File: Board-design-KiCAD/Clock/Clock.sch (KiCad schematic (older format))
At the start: 32 parts, among them M1 SevSeg4Inch, M2 SevSeg4Inch, U1 ULN2003A, U2 ULN2003A, U3 74HC595, U4 74HC595, U6 74HC595, Y1 SevSeg1.8Inch, Y2 SevSeg1.8Inch, Y3 SevSeg1.8Inch, Y4 SevSeg1.8Inch

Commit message: Add new tracks
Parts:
- added 5V-Cin1: 0.22uF - 50V, Capacitor_THT:CP_Radial_D4.0mm_P2.00mm, symbol Device:CP1
- added 5V-Cout1, 6V-Cout1: 0.1uF - 50V, Capacitor_THT:CP_Radial_D5.0mm_P2.00mm, symbol Device:CP1
- added 6V-Cin1: 0.33uF - 50V, Capacitor_THT:CP_Radial_D4.0mm_P2.00mm, symbol Device:CP1
- added CommonPinControl_YEAR1: ULN2003A, Package_DIP:DIP-16_W7.62mm_Socket_LongPads, symbol Transistor_Array:ULN2003A
- added RDP1, RDP2: 680, Resistor_THT:R_Axial_DIN0207_L6.3mm_D2.5mm_P10.16mm_Horizontal, symbol Device:R_US
- added Regulator-5V1: LM7805_TO220, Package_TO_SOT_THT:TO-220-3_Horizontal_TabDown, symbol Regulator_Linear:LM7805_TO220
- added Regulator-6V1: L7806, Package_TO_SOT_THT:TO-220-3_Horizontal_TabDown, symbol Regulator_Linear:L7806
- BCD-TIME1: renamed from BCD-YEAR1; footprint Package_DIP:DIP-18_W7.62mm_LongPads -> Package_DIP:DIP-16_W7.62mm_Socket_LongPads
- CommonPinControl_TIME1: renamed from CommonPinControl1; footprint Package_DIP:DIP-18_W7.62mm_LongPads -> Package_DIP:DIP-16_W7.62mm_Socket_LongPads
- DATE_INPUT_CONTROL1: renamed from U6; footprint (none) -> Package_DIP:DIP-16_W7.62mm_Socket_LongPads
- InputPowerConverter1: footprint Package_DIP:DIP-18_W7.62mm_LongPads -> Package_DIP:DIP-16_W7.62mm_Socket_LongPads
- TIME_INPUT_CONTROL1: renamed from U3; footprint (none) -> Package_DIP:DIP-16_W7.62mm_Socket_LongPads
- YEAR_INPUT_CONTROL1: renamed from U4; footprint (none) -> Package_DIP:DIP-16_W7.62mm_Socket_LongPads
- renumbered BCD-TIME1 to BCD-YEAR1
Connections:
- net +11V: now also 5V-Cin1.1, 6V-Cin1.1, Regulator-5V1.1 (VI), Regulator-6V1.1 (IN)
- net GND: now also BCD-YEAR1.8 (GND), TIME_INPUT_CONTROL1.8 (GND), YEAR_INPUT_CONTROL1.8 (GND), 5V-Cin1.2, 5V-Cout1.2, 6V-Cin1.2, 6V-Cout1.2, CommonPinControl_YEAR1.8 (GND), Regulator-5V1.2 (GND), Regulator-6V1.2 (GND)
- net H1_EN: now reaches H1.1 (GND), H1.8 (GND)
- net H1_EN: now also CommonPinControl_TIME1.16 (O1)
- net H2_EN: now reaches H2.1 (GND), H2.8 (GND)
- net H2_EN: now also CommonPinControl_TIME1.15 (O2)
- net at H2.5 (DP): now also RDP1.1
- net H3_EN: now reaches M1.1 (GND), M1.8 (GND)
- net H3_EN: now also CommonPinControl_TIME1.14 (O3)
- net at M1.5 (DP): now also RDP2.1
- net H4_EN: now reaches M2.1 (GND), M2.8 (GND)
- net H4_EN: now also CommonPinControl_TIME1.13 (O4)
- net Y1_EN: now reaches Y1.1 (Vdd), Y1.5 (Vdd)
- net Y1_EN: now also CommonPinControl_YEAR1.16 (O1)
- net YEAR_G: now reaches Y1.10 (G)
- net YEAR_G: now also BCD-YEAR1.14 (g), Y2.10 (G), Y3.10 (G), Y4.10 (G)
- net YEAR_E: now reaches Y1.2 (E)
- net YEAR_E: now also BCD-YEAR1.9 (e), Y2.2 (E), Y3.2 (E), Y4.2 (E)
- net YEAR_D: now reaches Y1.3 (D)
- net YEAR_D: now also BCD-YEAR1.10 (d), Y2.3 (D), Y3.3 (D), Y4.3 (D)
- net YEAR_C: now reaches Y1.4 (C)
- net YEAR_C: now also BCD-YEAR1.11 (c), Y2.4 (C), Y3.4 (C), Y4.4 (C)
- net YEAR_B: now reaches Y1.6 (B)
- net YEAR_B: now also BCD-YEAR1.12 (b), Y2.6 (B), Y3.6 (B), Y4.6 (B)
- net YEAR_A: now reaches Y1.7 (A)
- net YEAR_A: now also BCD-YEAR1.13 (a), Y2.7 (A), Y3.7 (A), Y4.7 (A)
- net YEAR_F: now reaches Y1.9 (F)
- net YEAR_F: now also BCD-YEAR1.15 (f), Y2.9 (F), Y3.9 (F), Y4.9 (F)
- net Y2_EN: now reaches Y2.1 (Vdd), Y2.5 (Vdd)
- net Y2_EN: now also CommonPinControl_YEAR1.15 (O2)
- net Y3_EN: now reaches Y3.1 (Vdd), Y3.5 (Vdd)
- net Y3_EN: now also CommonPinControl_YEAR1.14 (O3)
- net Y4_EN: now reaches Y4.1 (Vdd), Y4.5 (Vdd)
- net Y4_EN: now also CommonPinControl_YEAR1.13 (O4)
- net at BCD-TIME1.1 (B): now also TIME_INPUT_CONTROL1.1 (QB)
- net +6V: now reaches BCD-TIME1.16 (VCC)
- net +6V: now also BCD-YEAR1.16 (VCC), 6V-Cout1.1, CommonPinControl_YEAR1.9 (COM), Regulator-6V1.3 (OUT)
- net at BCD-TIME1.2 (C): now also TIME_INPUT_CONTROL1.2 (QC)
- net +5V: now reaches BCD-TIME1.3 (LT)
- net +5V: now also BCD-TIME1.4 (BI), BCD-TIME1.5 (RBI), BCD-YEAR1.3 (LT), BCD-YEAR1.4 (BI), BCD-YEAR1.5 (RBI), TIME_INPUT_CONTROL1.16 (VCC), YEAR_INPUT_CONTROL1.16 (VCC), 5V-Cout1.1, Regulator-5V1.3 (VO)
- net at BCD-TIME1.6 (D): now also TIME_INPUT_CONTROL1.3 (QD)
- net at BCD-TIME1.7 (A): now also TIME_INPUT_CONTROL1.15 (QA)
- net at YEAR_INPUT_CONTROL1.1 (QB): now also BCD-YEAR1.1 (B)
- net at YEAR_INPUT_CONTROL1.15 (QA): now also BCD-YEAR1.7 (A)
- net at YEAR_INPUT_CONTROL1.2 (QC): now also BCD-YEAR1.2 (C)
- net at YEAR_INPUT_CONTROL1.3 (QD): now also BCD-YEAR1.6 (D)
- net EN_DIGIT_1: now reaches CommonPinControl_TIME1.1 (I1)
- net DP_EN: now reaches CommonPinControl_TIME1.12 (O5)
- net DP_EN: now also RDP1.2, RDP2.2
- net EN_DIGIT_2: now reaches CommonPinControl_TIME1.2 (I2)
- net EN_DIGIT_3: now reaches CommonPinControl_TIME1.3 (I3)
- net EN_DIGIT_4: now reaches CommonPinControl_TIME1.4 (I4)
- new net INVERTED_EN_DIGIT_1: CommonPinControl_YEAR1.1 (I1)
- new net INVERTED_EN_DIGIT_2: CommonPinControl_YEAR1.2 (I2)
- new net INVERTED_EN_DIGIT_3: CommonPinControl_YEAR1.3 (I3)
- new net INVERTED_EN_DIGIT_4: CommonPinControl_YEAR1.4 (I4)
- no-connect marks 11 -> 21
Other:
- moved on the sheet: BCD-TIME1, BCD-YEAR1, Cff1, Cin1, CommonPinControl_TIME1, Cout1, DATE_INPUT_CONTROL1, Diode1, H1, H2, InputPowerConverter1, L1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

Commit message: Add some display wirings
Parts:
- removed D1, D2, Mo1, Mo2: SevSeg1.8Inch, Custom:SevSeg1.8Inch, symbol Custom:SevSeg1.8Inch
- removed U1, U2: ULN2003A, symbol Transistor_Array:ULN2003A
- added CommonPinControl_DATE1: ULN2003A, Package_DIP:DIP-16_W7.62mm_Socket_LongPads, symbol Transistor_Array:ULN2003A
- added Da_1, Da_2, Mo_1, Mo_2: SevSeg1.8Inch, Custom:SevSeg1.8Inch, symbol Custom:SevSeg1.8Inch
- added INVERTER_1, INVERTER_2: 74HC14, Package_DIP:DIP-14_W7.62mm_Socket_LongPads, symbol 74xx:74HC14
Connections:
- net INVERTED_EN_DIGIT_1 is gone; now on net EN_DIGIT_1: CommonPinControl_YEAR1.1 (I1)
- net INVERTED_EN_DIGIT_2 is gone; now on net EN_DIGIT_2: CommonPinControl_YEAR1.2 (I2)
- net INVERTED_EN_DIGIT_3 is gone; now on net EN_DIGIT_3: CommonPinControl_YEAR1.3 (I3)
- net INVERTED_EN_DIGIT_4 is gone; now on net EN_DIGIT_4: CommonPinControl_YEAR1.4 (I4)
- net +5V: now also BCD-TIME1.16 (VCC), DATE_INPUT_CONTROL1.10 (~SRCLR), DATE_INPUT_CONTROL1.16 (VCC), TIME_INPUT_CONTROL1.10 (~SRCLR), YEAR_INPUT_CONTROL1.10 (~SRCLR), INVERTER_1.14 (VCC), INVERTER_2.14 (VCC); no longer BCD-YEAR1.3 (LT), BCD-YEAR1.4 (BI), BCD-YEAR1.5 (RBI)
- net +6V: now also BCD-DATE1.16 (VCC), BCD-DATE1.3 (LT), BCD-DATE1.4 (BI), BCD-DATE1.5 (RBI), BCD-YEAR1.3 (LT), BCD-YEAR1.4 (BI), BCD-YEAR1.5 (RBI), CommonPinControl_DATE1.9 (COM); no longer BCD-TIME1.16 (VCC)
- net EN_DIGIT_1: now also CommonPinControl_DATE1.1 (I1), INVERTER_2.3; no longer CommonPinControl_TIME1.1 (I1)
- net EN_DIGIT_2: now also CommonPinControl_DATE1.2 (I2), INVERTER_2.5; no longer CommonPinControl_TIME1.2 (I2)
- net EN_DIGIT_3: now also CommonPinControl_DATE1.3 (I3), INVERTER_2.9; no longer CommonPinControl_TIME1.3 (I3)
- net EN_DIGIT_4: now also CommonPinControl_DATE1.4 (I4), INVERTER_2.11; no longer CommonPinControl_TIME1.4 (I4)
- net GND: now also BCD-DATE1.8 (GND), DATE_INPUT_CONTROL1.13 (~OE), DATE_INPUT_CONTROL1.8 (GND), TIME_INPUT_CONTROL1.13 (~OE), YEAR_INPUT_CONTROL1.13 (~OE), CommonPinControl_DATE1.8 (GND), INVERTER_1.7 (GND), INVERTER_2.7 (GND)
- net PWR_TIME_D: now reaches InputPowerConverter1.4 (I4)
- net PWR_TIME_D: now also INVERTER_1.8; no longer BCD-TIME1.10 (d)
- net PWR_TIME_C: now reaches InputPowerConverter1.3 (I3)
- net PWR_TIME_C: now also INVERTER_1.6; no longer BCD-TIME1.11 (c)
- net PWR_TIME_B: now reaches InputPowerConverter1.2 (I2)
- net PWR_TIME_B: now also INVERTER_1.4; no longer BCD-TIME1.12 (b)
- net PWR_TIME_A: now reaches InputPowerConverter1.1 (I1)
- net PWR_TIME_A: now also INVERTER_1.2; no longer BCD-TIME1.13 (a)
- net PWR_TIME_G: now reaches InputPowerConverter1.7 (I7)
- net PWR_TIME_G: now also INVERTER_2.2; no longer BCD-TIME1.14 (g)
- net PWR_TIME_F: now reaches InputPowerConverter1.6 (I6)
- net PWR_TIME_F: now also INVERTER_1.12; no longer BCD-TIME1.15 (f)
- net PWR_TIME_E: now reaches InputPowerConverter1.5 (I5)
- net PWR_TIME_E: now also INVERTER_1.10; no longer BCD-TIME1.9 (e)
- net CLOCK: now reaches TIME_INPUT_CONTROL1.11 (SRCLK)
- net CLOCK: now also DATE_INPUT_CONTROL1.11 (SRCLK), YEAR_INPUT_CONTROL1.11 (SRCLK)
- net LATCH: now reaches TIME_INPUT_CONTROL1.12 (RCLK)
- net LATCH: now also DATE_INPUT_CONTROL1.12 (RCLK), YEAR_INPUT_CONTROL1.12 (RCLK)
- net TIME_DATA_INPUT: now reaches TIME_INPUT_CONTROL1.14 (SER)
- net YEAR_DATA_INPUT: now reaches YEAR_INPUT_CONTROL1.14 (SER)
- net at DATE_INPUT_CONTROL1.1 (QB): now also BCD-DATE1.1 (B)
- net DATE_DATA_INPUT: now reaches DATE_INPUT_CONTROL1.14 (SER)
- net at DATE_INPUT_CONTROL1.15 (QA): now also BCD-DATE1.7 (A)
- net at DATE_INPUT_CONTROL1.2 (QC): now also BCD-DATE1.2 (C)
- net at DATE_INPUT_CONTROL1.3 (QD): now also BCD-DATE1.6 (D)
- net DP_PWM: now reaches CommonPinControl_TIME1.5 (I5)
- net DATE_D: now reaches BCD-DATE1.10 (d)
- net DATE_D: now also Da_1.3 (D), Da_2.3 (D), Mo_1.3 (D), Mo_2.3 (D)
- net DATE_C: now reaches BCD-DATE1.11 (c)
- net DATE_C: now also Da_1.4 (C), Da_2.4 (C), Mo_1.4 (C), Mo_2.4 (C)
- net DATE_B: now reaches BCD-DATE1.12 (b)
- net DATE_B: now also Da_1.6 (B), Da_2.6 (B), Mo_1.6 (B), Mo_2.6 (B)
- net DATE_A: now reaches BCD-DATE1.13 (a)
- net DATE_A: now also Da_1.7 (A), Da_2.7 (A), Mo_1.7 (A), Mo_2.7 (A)
- net DATE_G: now reaches BCD-DATE1.14 (g)
- net DATE_G: now also Da_1.10 (G), Da_2.10 (G), Mo_1.10 (G), Mo_2.10 (G)
- net DATE_F: now reaches BCD-DATE1.15 (f)
- net DATE_F: now also Da_1.9 (F), Da_2.9 (F), Mo_1.9 (F), Mo_2.9 (F)
- net DATE_E: now reaches BCD-DATE1.9 (e)
- net DATE_E: now also Da_1.2 (E), Da_2.2 (E), Mo_1.2 (E), Mo_2.2 (E)
- new net: CommonPinControl_TIME1.1 (I1), INVERTER_2.4
- new net: CommonPinControl_TIME1.2 (I2), INVERTER_2.6
- new net: CommonPinControl_TIME1.3 (I3), INVERTER_2.8
- new net: CommonPinControl_TIME1.4 (I4), INVERTER_2.10
- new net Da1_EN: CommonPinControl_DATE1.16 (O1), Da_1.1 (Vdd), Da_1.5 (Vdd)
- new net Da2_EN: CommonPinControl_DATE1.15 (O2), Da_2.1 (Vdd), Da_2.5 (Vdd)
- new net Mo1_EN: CommonPinControl_DATE1.14 (O3), Mo_1.1 (Vdd), Mo_1.5 (Vdd)
- new net Mo2_EN: CommonPinControl_DATE1.13 (O4), Mo_2.1 (Vdd), Mo_2.5 (Vdd)
- new net SIGNAL_TIME_A: BCD-TIME1.13 (a), INVERTER_1.1
- new net SIGNAL_TIME_B: BCD-TIME1.12 (b), INVERTER_1.3
- new net SIGNAL_TIME_C: BCD-TIME1.11 (c), INVERTER_1.5
- new net SIGNAL_TIME_D: BCD-TIME1.10 (d), INVERTER_1.9
- new net SIGNAL_TIME_E: BCD-TIME1.9 (e), INVERTER_1.11
- new net SIGNAL_TIME_F: BCD-TIME1.15 (f), INVERTER_1.13
- new net SIGNAL_TIME_G: BCD-TIME1.14 (g), INVERTER_2.1
- no-connect marks 21 -> 42
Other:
- moved on the sheet: 5V-Cin1, 5V-Cout1, 6V-Cin1, 6V-Cout1, BCD-TIME1, BCD-YEAR1, Cff1, Cin1, CommonPinControl_TIME1, CommonPinControl_YEAR1, Cout1, Diode1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

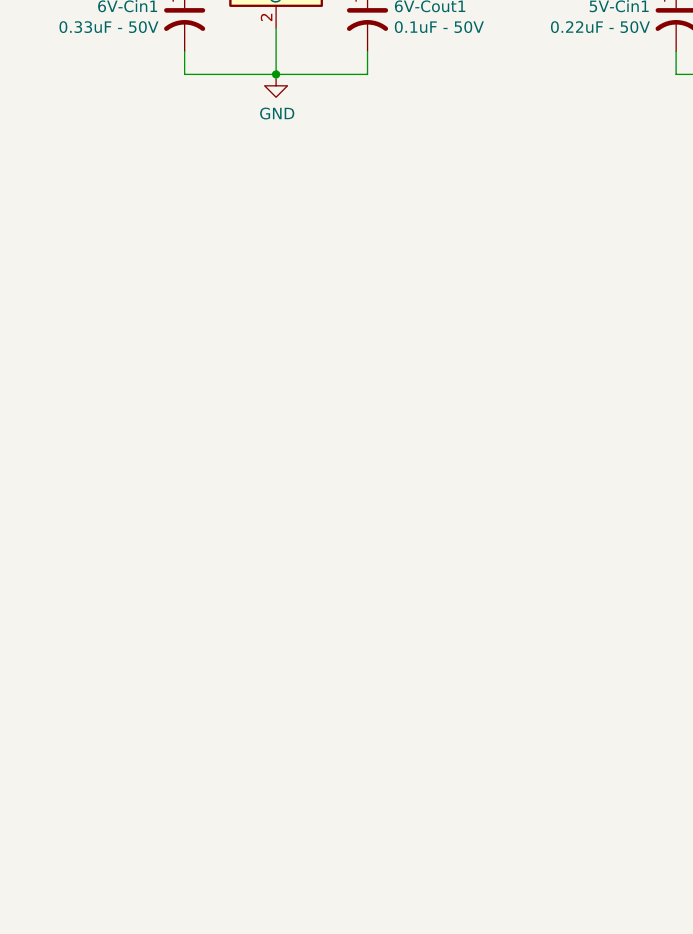
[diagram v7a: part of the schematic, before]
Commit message: Add Blue Pill to schematics
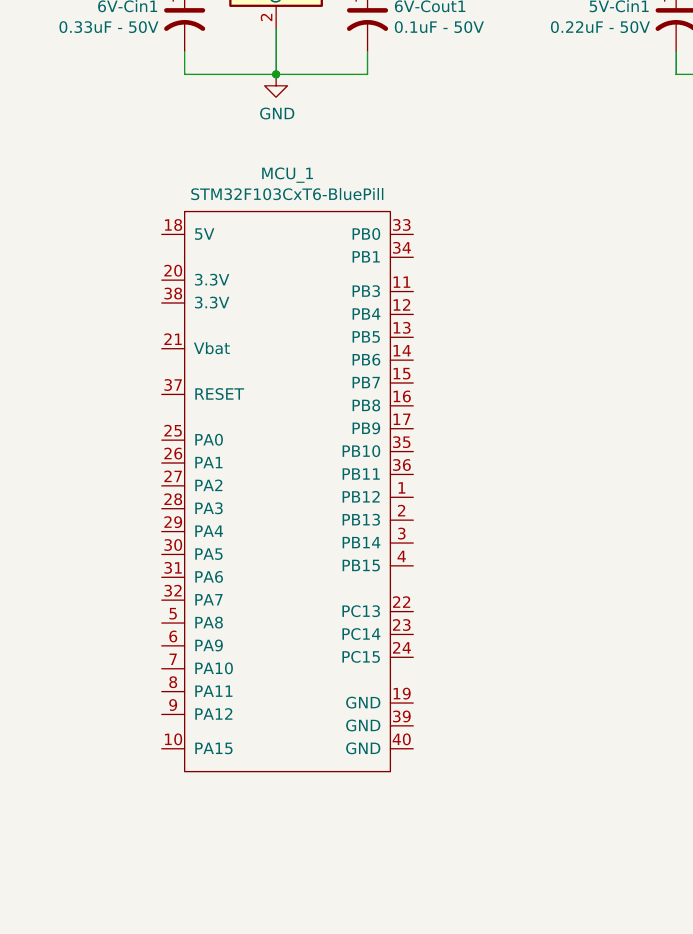
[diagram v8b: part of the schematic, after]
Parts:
- added MCU_1: STM32F103CxT6-BluePill, Custom:STM32F103CxT6-BluePill, symbol Custom:STM32F103CxT6-BluePill
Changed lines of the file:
@@
 Wire Bus Line
 	8800 7200 8800 8300
+$Comp
+L Custom:STM32F103CxT6-BluePill MCU_1
+U 1 1 60511CCC
+P 1900 4850
+F 0 "MCU_1" H 1900 6215 50  0000 C CNN
+F 1 "STM32F103CxT6-BluePill" H 1900 6124 50  0000 C CNN
+F 2 "Custom:STM32F103CxT6-BluePill" H 1850 5400 50  0001 C CNN
+F 3 "" H 1850 5400 50  0001 C CNN
+	1    1900 4850
+	1    0    0    -1
+$EndComp
 $EndSCHEMATC
